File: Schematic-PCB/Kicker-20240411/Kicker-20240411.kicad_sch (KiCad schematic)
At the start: 10 parts, among them J1 Conn_01x02_Pin, J2 Conn_01x05_Pin, J3 Conn_01x02_Pin, Q1 NMOS

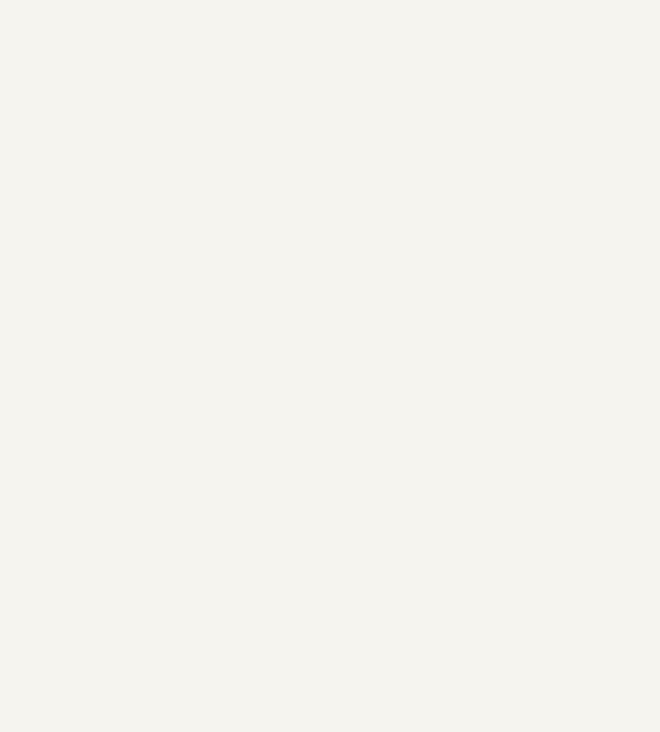
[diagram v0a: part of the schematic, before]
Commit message: キッカーの回路図を修正しました
DR 2024.04.11を参考にキッカー基板を修正しました
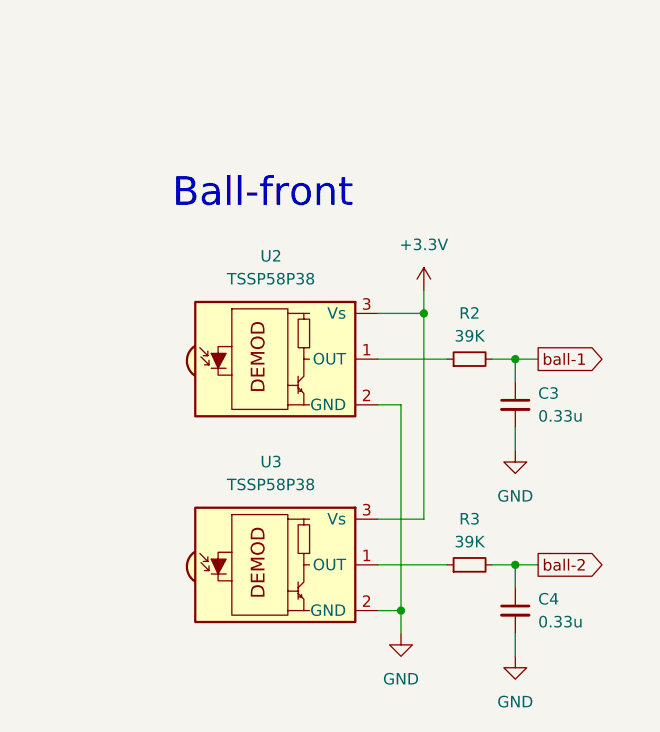
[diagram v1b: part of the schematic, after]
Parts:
- added C3, C4: 0.33u, symbol Device:C_Small
- added R2, R3: 39K, symbol Device:R_Small
- added U2, U3: TSSP58P38, OptoDevice:Vishay_MINICAST-3Pin, symbol Sensor_Proximity:TSSP58P38
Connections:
- net +3.3V: now also U2.3 (Vs), U3.3 (Vs)
- net GND: now also C3.2, C4.2, U2.2 (GND), U3.2 (GND)
- net ball-1: now also C3.1, R2.2
- net ball-2: now also C4.1, R3.2
- new net: R2.1, U2.1 (OUT)
- new net: R3.1, U3.1 (OUT)
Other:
- note added: "Ball-front"

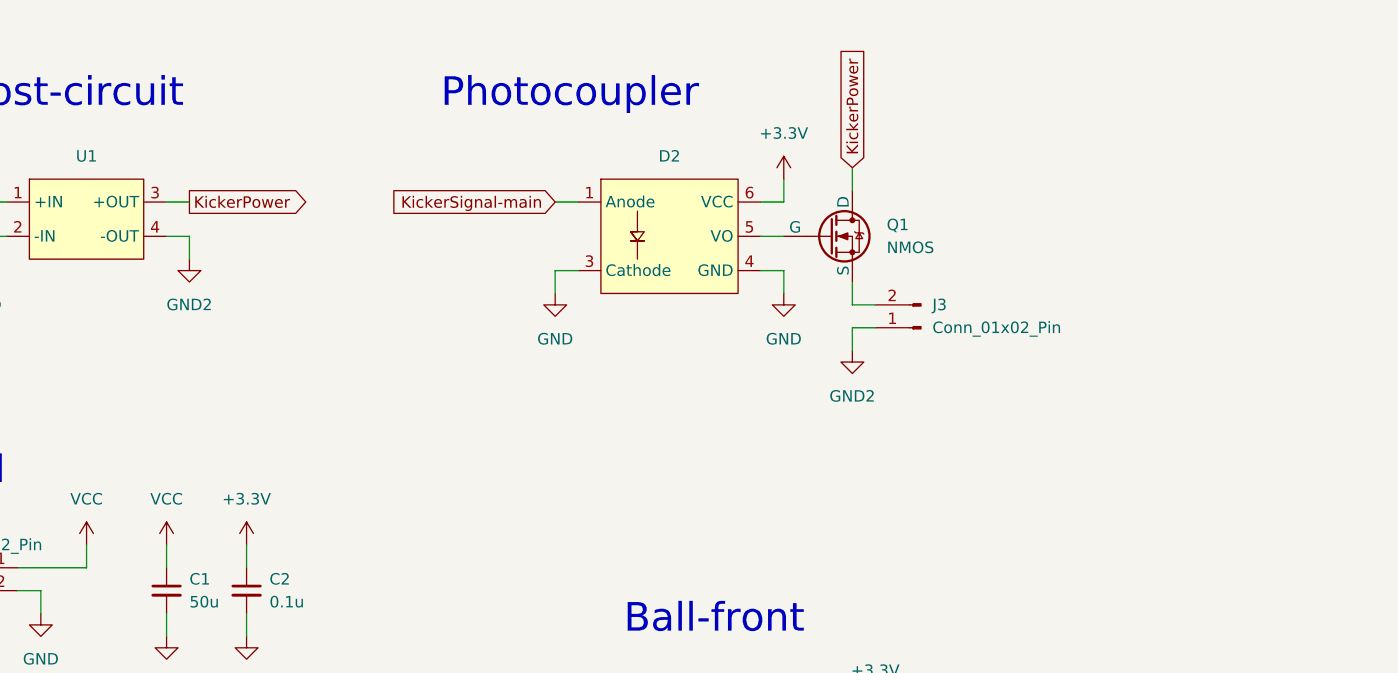
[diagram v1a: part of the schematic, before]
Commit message: キッカー基板のPCBを作成
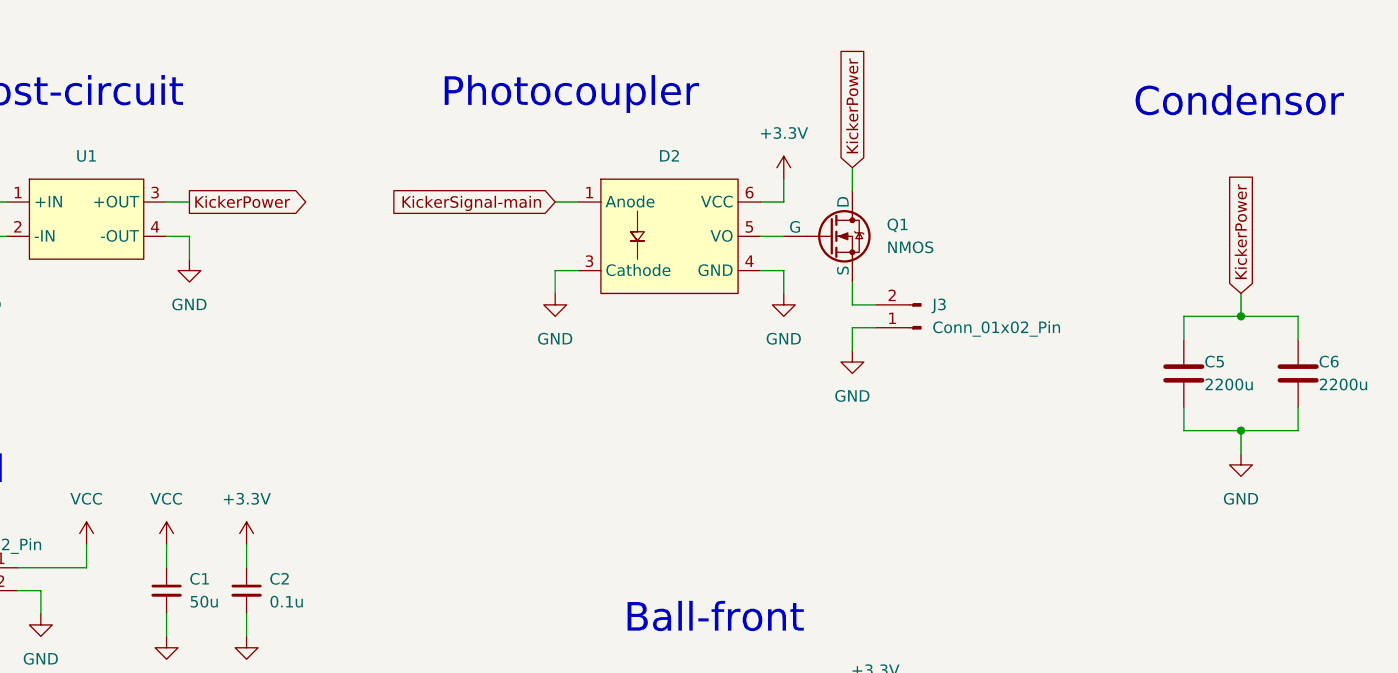
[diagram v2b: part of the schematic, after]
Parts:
- added C5, C6: 2200u, Capacitor_THT:CP_Radial_D16.0mm_P7.50mm, symbol Device:C
- C1: footprint (none) -> Capacitor_SMD:C_0805_2012Metric
- C2, C3, C4: footprint (none) -> Capacitor_SMD:C_0603_1608Metric
- D1: footprint (none) -> LED_SMD:LED_0805_2012Metric
- D2: footprint (none) -> Package_SO:SO-5_4.4x3.6mm_P1.27mm
- J1: footprint (none) -> Connector_JST:JST_XH_B2B-XH-A_1x02_P2.50mm_Vertical
- J2: footprint (none) -> Connector_JST:JST_XH_S5B-XH-A-1_1x05_P2.50mm_Horizontal
- J3: footprint (none) -> Connector_JST:JST_XH_S2B-XH-A-1_1x02_P2.50mm_Horizontal
- Q1: footprint (none) -> Package_TO_SOT_SMD:TO-252-2
- R1, R2, R3: footprint (none) -> Resistor_SMD:R_0603_1608Metric
- U1: footprint (none) -> @MyLibrary:XL6009
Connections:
- net GND2 is gone; now on net GND: J3.1 (Pin_1), U1.4 (-OUT)
- net GND: now also C5.2, C6.2
- net KickerPower: now also C5.1, C6.1
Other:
- note added: "Condensor"

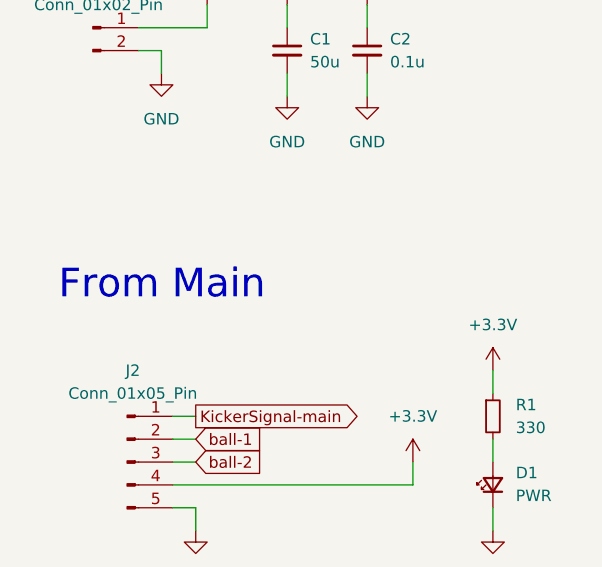
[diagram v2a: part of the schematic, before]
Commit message: キッカー・MD・ラインセンサ・電源基板を更新
キッカー :
・基板外形変更後のPCBの修正が途中で止まっていたため、残りの部分を編集した

ラインセンサ :
・以前のラインセンサ回路を、コンパレータを使用する回路へと置換した
・ラベル line_threshold を、PWM出力可能な5番ピンに設定した

MD :
・キッカーもMD基板を経由させるように変更した
・ラインセンサ用にレベル変換回路を作成した

電源基板 :
・フットプリントを一部指定した
・基板外形をインポートした
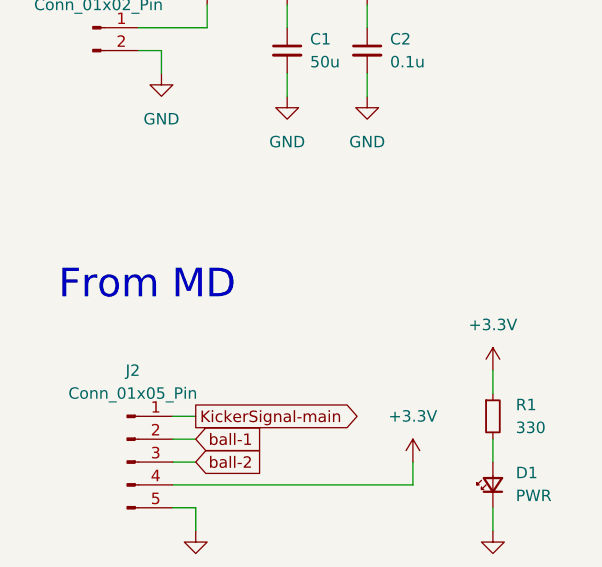
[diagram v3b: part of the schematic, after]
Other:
- note added: "From MD"
- note removed: "From Main"
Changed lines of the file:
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@@
 		)
 	)
-	(text "From Main"
+	(text "From MD"
 		(exclude_from_sim no)
 		(at 20.32 106.68 0)

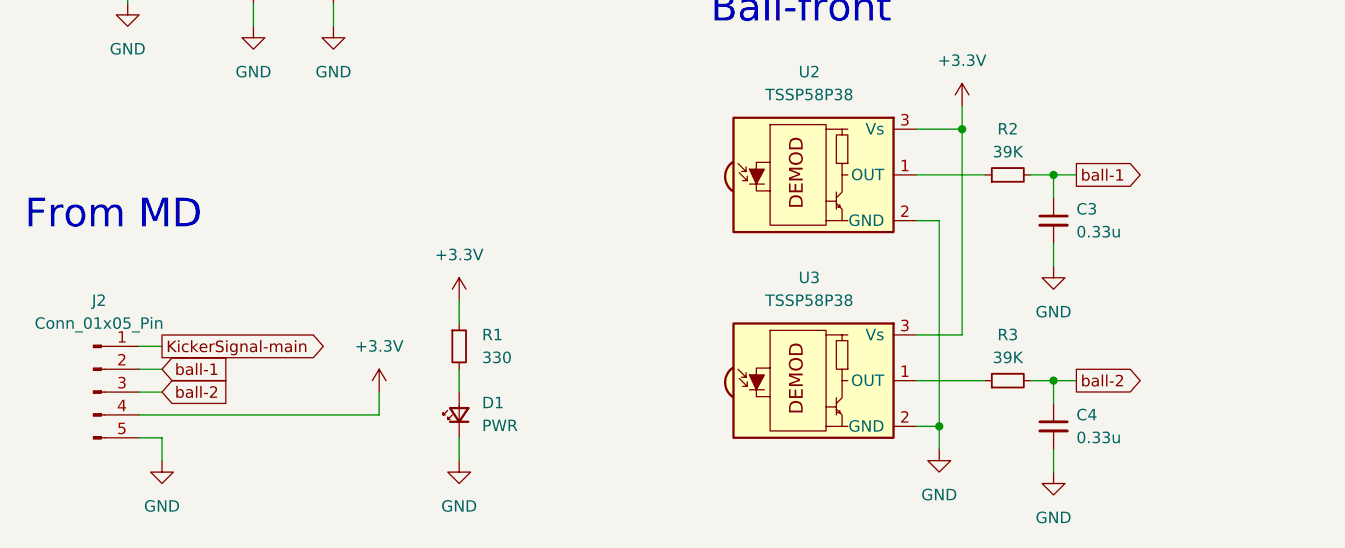
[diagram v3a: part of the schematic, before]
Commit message: MD基板・メイン基板の回路図を更新
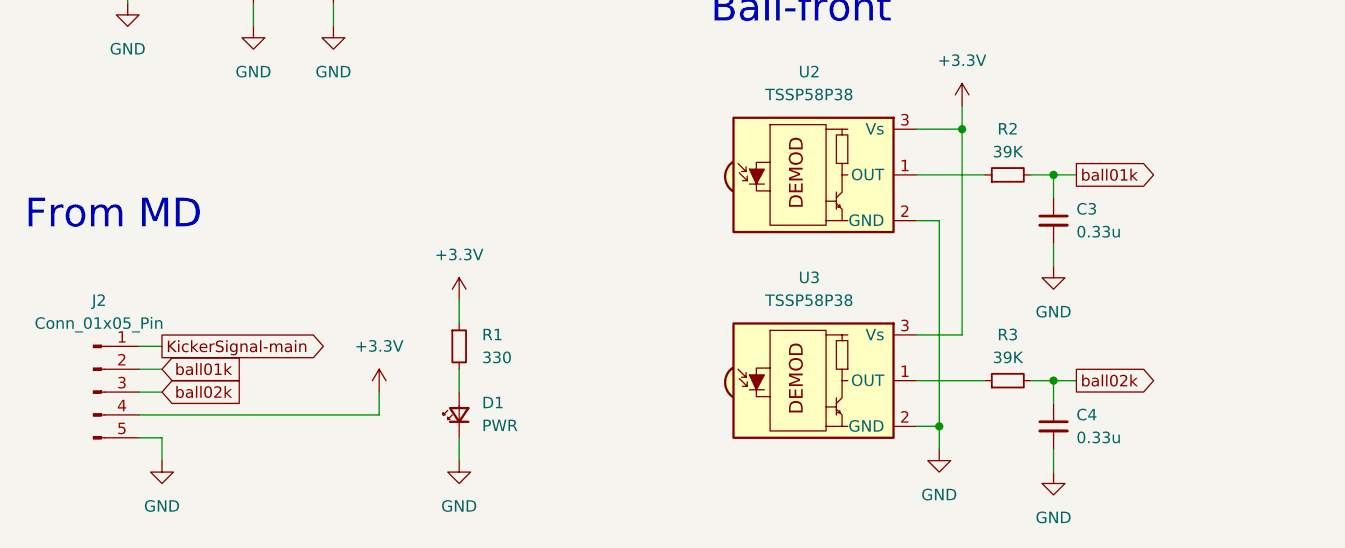
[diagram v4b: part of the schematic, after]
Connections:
- net ball-1 renamed ball01k
- net ball-2 renamed ball02k
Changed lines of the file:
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@@
 		)
 	)
-	(global_label "ball-1"
+	(global_label "ball01k"
 		(shape input)
 		(at 35.56 121.92 0)
@@
 		)
 		(property "Intersheetrefs" "${INTERSHEET_REFS}"
-			(at 43.653 121.92 0)
+			(at 45.6207 121.92 0)
 			(effects
 				(font
@@
 		)
 	)
-	(global_label "ball-2"
+	(global_label "ball02k"
 		(shape input)
 		(at 35.56 124.46 0)
@@
 		)
 		(property "Intersheetrefs" "${INTERSHEET_REFS}"
-			(at 43.653 124.46 0)
+			(at 45.6207 124.46 0)
 			(effects
 				(font
@@
 		)
 	)
-	(global_label "ball-2"
+	(global_label "ball02k"
 		(shape output)
 		(at 137.16 123.19 0)
@@
 		)
 		(property "Intersheetrefs" "${INTERSHEET_REFS}"
-			(at 145.253 123.19 0)
+			(at 147.2207 123.19 0)
 			(effects
 				(font
@@
 		)
 	)
-	(global_label "ball-1"
+	(global_label "ball01k"
 		(shape output)
 		(at 137.16 100.33 0)
@@
 		)
 		(property "Intersheetrefs" "${INTERSHEET_REFS}"
-			(at 145.253 100.33 0)
+			(at 147.2207 100.33 0)
 			(effects
 				(font

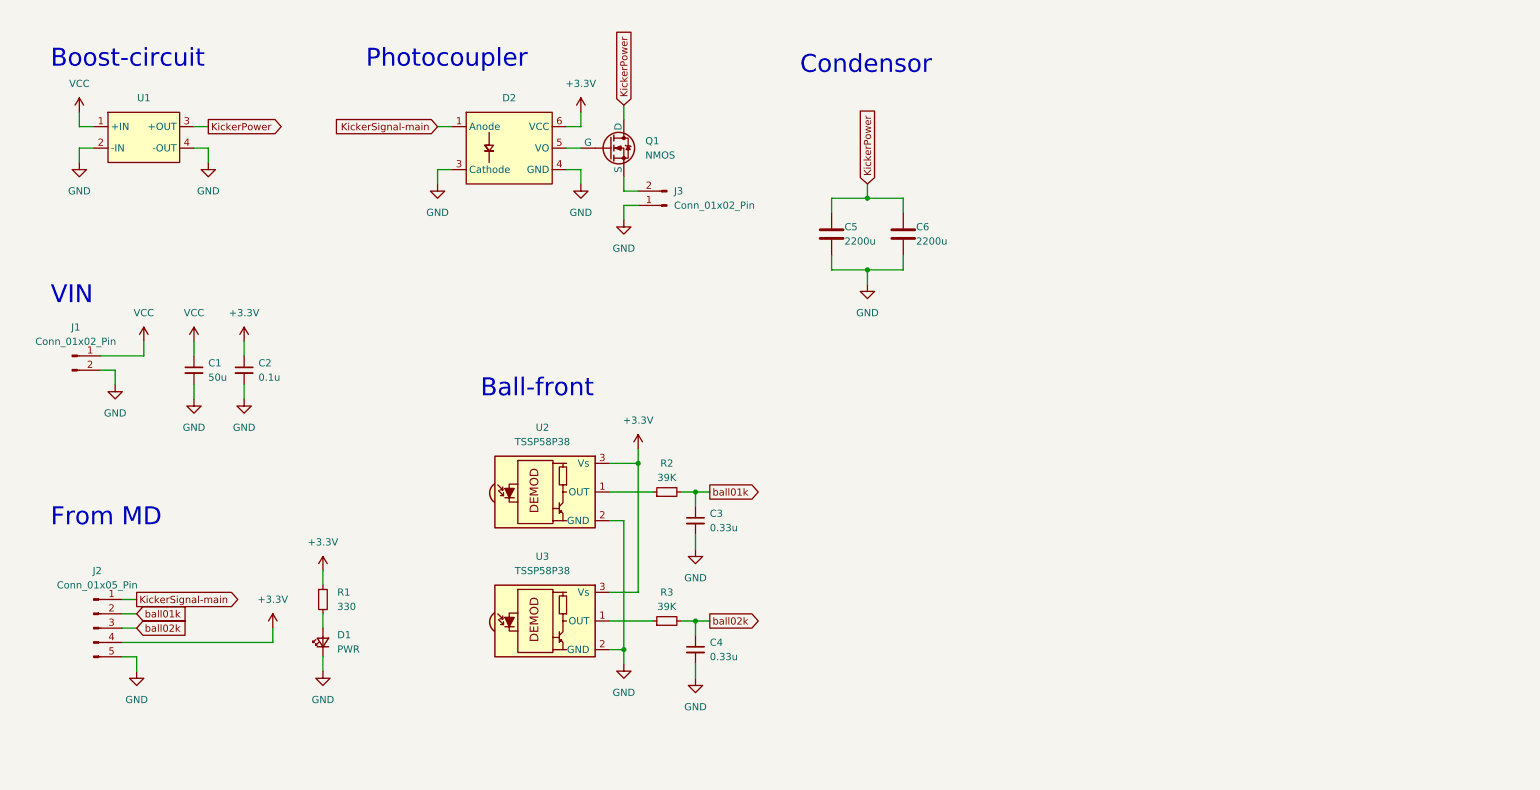
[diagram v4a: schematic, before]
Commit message: キッカー基板 回路図の変更
DRをお願いします。
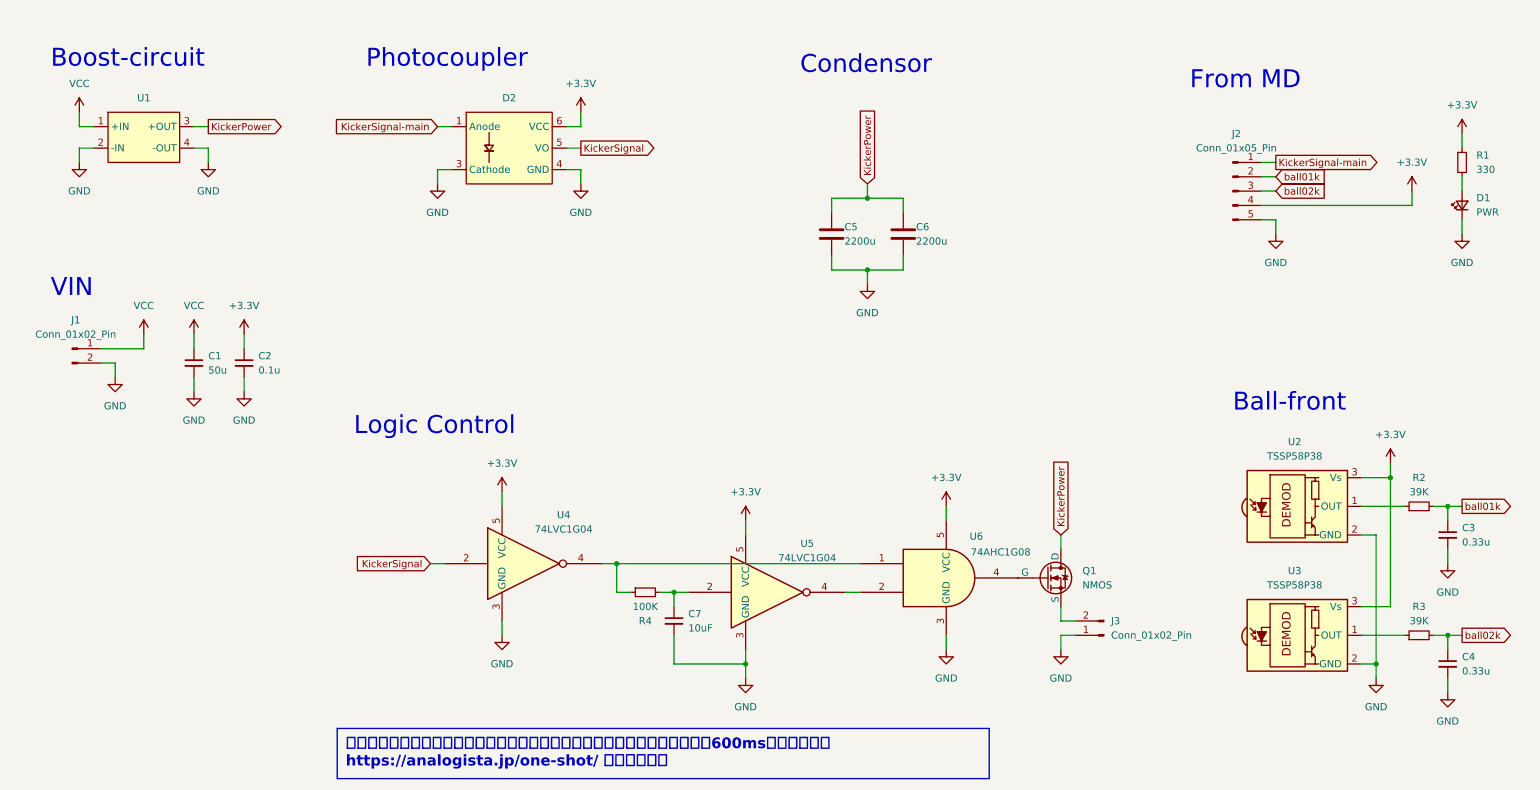
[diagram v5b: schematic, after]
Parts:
- added C7: 10uF, symbol Device:C_Small
- added R4: 100K, symbol Device:R_Small
- added U4, U5: 74LVC1G04, symbol 74xGxx:74LVC1G04
- added U6: 74AHC1G08, symbol 74xGxx:74AHC1G08
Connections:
- net +3.3V: now also U4.5 (VCC), U5.5 (VCC), U6.5 (VCC)
- net GND: now also C7.2, U4.3 (GND), U5.3 (GND), U6.3 (GND)
- net at Q1.1 (G): now also U6.4; no longer D2.5 (VO)
- new net: R4.1, U4.4, U6.1
- new net: C7.1, R4.2, U5.2
- new net: U5.4, U6.2
- new net KickerSignal: D2.5 (VO), U4.2
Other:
- note added: "Logic Control"
- moved on the sheet: C1, C2, C3, C4, D1, J1, J2, J3, Q1, R1, R2, R3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

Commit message: Auto stash before merge of "main" and "origin/main"
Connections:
- net +3.3V: now also J2.3 (Pin_3); no longer J2.4 (Pin_4)
- net GND: now also J2.4 (Pin_4); no longer J2.5 (Pin_5)
- net KickerSignal-main: now also J2.2 (Pin_2); no longer J2.1 (Pin_1)
- net ball01k: now also J2.5 (Pin_5); no longer J2.2 (Pin_2)
- net ball02k: now also J2.1 (Pin_1); no longer J2.3 (Pin_3)

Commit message: キッカー基盤のPCBを修正
回路図の変更に伴うPCBの修正
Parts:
- C7: footprint (none) -> Capacitor_SMD:C_0603_1608Metric
- J1: footprint Connector_JST:JST_XH_B2B-XH-A_1x02_P2.50mm_Vertical -> Connector_JST:JST_XH_S2B-XH-A-1_1x02_P2.50mm_Horizontal
- J2: footprint Connector_JST:JST_XH_S5B-XH-A-1_1x05_P2.50mm_Horizontal -> Connector_FFC-FPC:TE_84953-5_1x05-1MP_P1.0mm_Horizontal
- J3: footprint Connector_JST:JST_XH_S2B-XH-A-1_1x02_P2.50mm_Horizontal -> Connector_JST:JST_XH_B2B-XH-A_1x02_P2.50mm_Vertical
- R4: footprint (none) -> Resistor_SMD:R_0603_1608Metric
- U4, U5, U6: footprint (none) -> Package_TO_SOT_SMD:SOT-23-5
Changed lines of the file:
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@@
 			)
 		)
-		(property "Footprint" ""
+		(property "Footprint" "Resistor_SMD:R_0603_1608Metric"
 			(at 125.73 118.11 0)
 			(effects
@@
 			)
 		)
-		(property "Footprint" ""
+		(property "Footprint" "Capacitor_SMD:C_0603_1608Metric"
 			(at 130.81 123.19 0)
 			(effects
@@
 			)
 		)
-		(property "Footprint" "Connector_JST:JST_XH_S2B-XH-A-1_1x02_P2.50mm_Horizontal"
+		(property "Footprint" "Connector_JST:JST_XH_B2B-XH-A_1x02_P2.50mm_Vertical"
 			(at 207.01 125.73 0)
 			(effects
@@
 			)
 		)
-		(property "Footprint" ""
+		(property "Footprint" "Package_TO_SOT_SMD:SOT-23-5"
 			(at 179.07 115.57 0)
 			(effects
@@
 			)
 		)
-		(property "Footprint" ""
+		(property "Footprint" "Package_TO_SOT_SMD:SOT-23-5"
 			(at 105.41 113.03 0)
 			(effects
@@
 			)
 		)
-		(property "Footprint" "Connector_JST:JST_XH_B2B-XH-A_1x02_P2.50mm_Vertical"
+		(property "Footprint" "Connector_JST:JST_XH_S2B-XH-A-1_1x02_P2.50mm_Horizontal"
 			(at 24.13 74.93 0)
 			(effects
@@
 			)
 		)
-		(property "Footprint" ""
+		(property "Footprint" "Package_TO_SOT_SMD:SOT-23-5"
 			(at 148.59 118.11 0)
 			(effects
@@
 			)
 		)
-		(property "Footprint" "Connector_JST:JST_XH_S5B-XH-A-1_1x05_P2.50mm_Horizontal"
+		(property "Footprint" "Connector_FFC-FPC:TE_84953-5_1x05-1MP_P1.0mm_Horizontal"
 			(at 229.87 46.99 0)
 			(effects
